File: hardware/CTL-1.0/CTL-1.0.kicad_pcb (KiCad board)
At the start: 2 copper layers, 139.7 x 63.5 mm, 58 parts, among them J1 Conn_02x16_Top_Bottom, J10 Conn_02x06_Odd_Even, J2 Conn_02x05_Odd_Even, J3 Conn_01x03, J4 Conn_01x02, J5 Conn_02x06_Odd_Even, J6 Conn_01x04, J7 Conn_01x04, J8 Conn_01x04, J9 Conn_01x06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

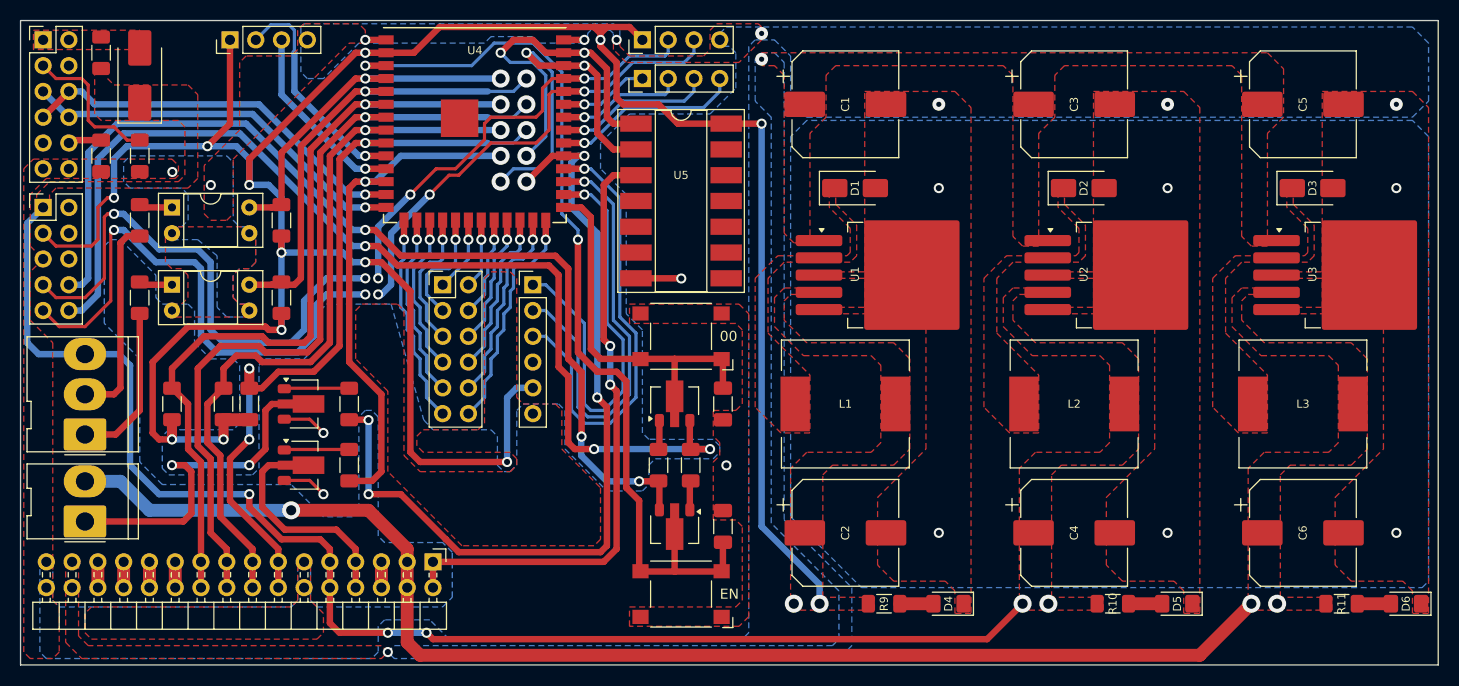
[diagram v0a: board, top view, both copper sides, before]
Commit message: modified:   .DS_Store 	modified:   README.md 	deleted:    hardware/CTL-1.0/CTL-1.0-backups/CTL-1.0-2025-05-23_140814.zip 	deleted:    hardware/CTL-1.0/CTL-1.0-backups/CTL-1.0-2025-05-23_142136.zip 	deleted:    hardware/CTL-1.0/CTL-1.0-backups/CTL-1.0-2025-05-23_145207.zip 	deleted:    hardware/CTL-1.0/CTL-1.0-backups/CTL-1.0-2025-05-23_145749.zip 	deleted:    hardware/CTL-1.0/CTL-1.0-backups/CTL-1.0-2025-06-03_185115.zip 	new file:   hardware/CTL-1.0/CTL-1.0-backups/CTL-1.0-2025-06-04_091843.zip 	new file:   hardware/CTL-1.0/CTL-1.0-backups/CTL-1.0-2025-06-04_105408.zip 	new file:   hardware/CTL-1.0/CTL-1.0-backups/CTL-1.0-2025-06-04_105918.zip 	new file:   hardware/CTL-1.0/CTL-1.0-backups/CTL-1.0-2025-06-04_110436.zip 	new file:   hardware/CTL-1.0/CTL-1.0-backups/CTL-1.0-2025-06-04_115049.zip 	new file:   hardware/CTL-1.0/CTL-1.0-backups/CTL-1.0-2025-06-04_132910.zip 	modified:   hardware/CTL-1.0/CTL-1.0.kicad_pcb 	modified:   hardware/CTL-1.0/CTL-1.0.kicad_prl 	modified:   hardware/CTL-1.0/CTL-1.0.kicad_sch 	new file:   hardware/PS-2.0/PS-2.0-backups/PS-2.0-2025-06-04_100004.zip 	new file:   hardware/PS-2.0/PS-2.0-backups/PS-2.0-2025-06-04_102434.zip 	new file:   hardware/PS-2.0/PS-2.0-backups/PS-2.0-2025-06-04_104734.zip 	new file:   hardware/PS-2.0/PS-2.0-backups/PS-2.0-2025-06-04_133345.zip 	modified:   hardware/PS-2.0/PS-2.0.kicad_pcb 	modified:   hardware/PS-2.0/PS-2.0.kicad_prl 	modified:   hardware/PS-2.0/PS-2.0.kicad_sch 	new file:   hardware/PS-2.0/~PS-2.0.kicad_pcb.lck 	new file:   hardware/PS-2.0/~PS-2.0.kicad_sch.lck 	modified:   pic/.DS_Store 	new file:   pic/PWM/Wave-pure-cut-driver-mosfet.png 	renamed:    pic/PWM/blend-cut-1/blend-cut-1-10.csv -> pic/PWM/blend-cut-1/CTL/blend-cut-1-10.csv 	renamed:    pic/PWM/blend-cut-1/blend-cut-1-10.png -> pic/PWM/blend-cut-1/CTL/blend-cut-1-10.png 	renamed:    pic/PWM/blend-cut-1/blend-cut-1-100.csv -> pic/PWM/blend-cut-1/CTL/blend-cut-1-100.csv 	renamed:    pic/PWM/blend-cut-1/blend-cut-1-100.png -> pic/PWM/ble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
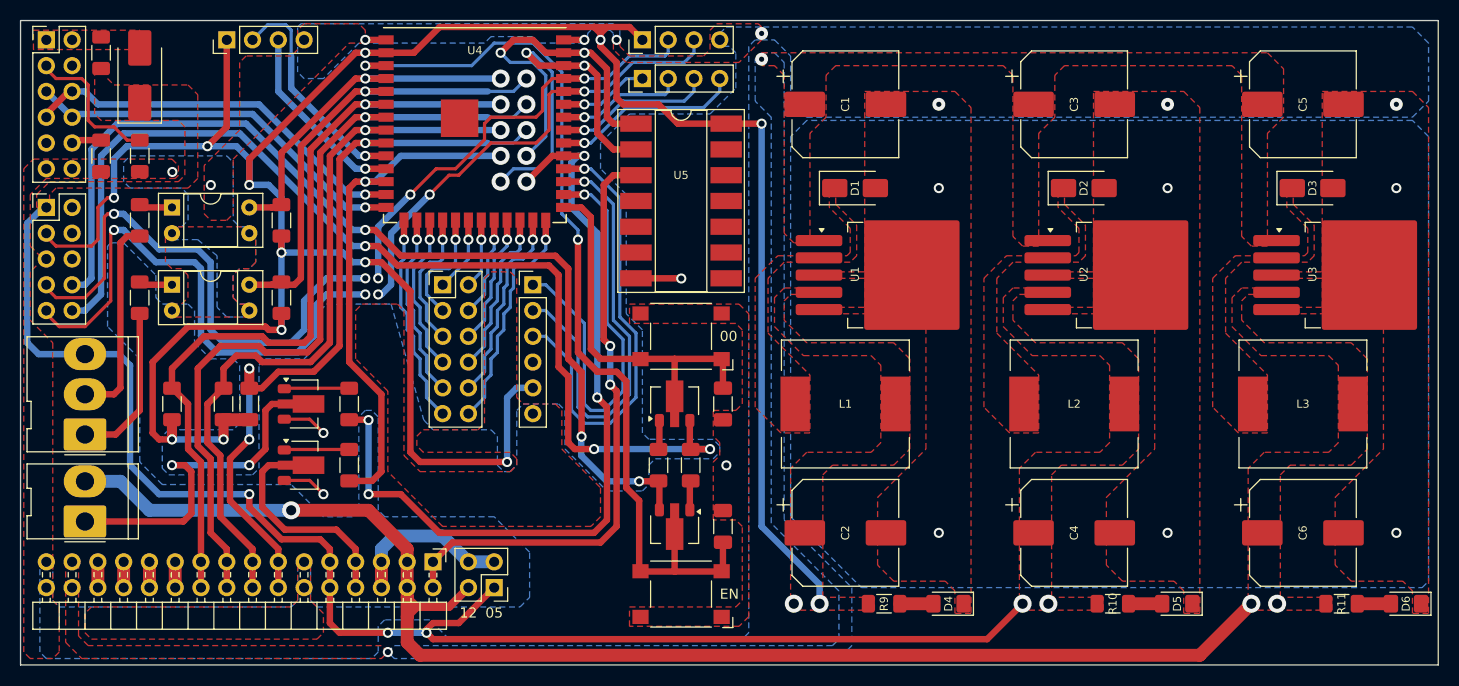
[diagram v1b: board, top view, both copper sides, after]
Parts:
- added J11: Conn_02x02_Odd_Even, Connector_PinHeader_2.54mm:PinHeader_2x02_P2.54mm_Vertical, F.Cu at (78.4, 151.1)
- moved J2 0.32 mm to (34.3, 113.7)
- moved J5 0.32 mm to (34.3, 97.2)
- moved J8 0.32 mm to (52.1, 97.2)
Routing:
- net /RLY-A: track 2.54 -> 16.5 mm
- net +5V: track 136.5 -> 145.2 mm
- net +12V: track 129.5 -> 138.1 mm
- net /CTL-BUZZ: track 83.0 -> 80.0 mm
- net /PWM: track 61.1 -> 59.8 mm
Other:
- board text added: "05"
- board text added: "12"

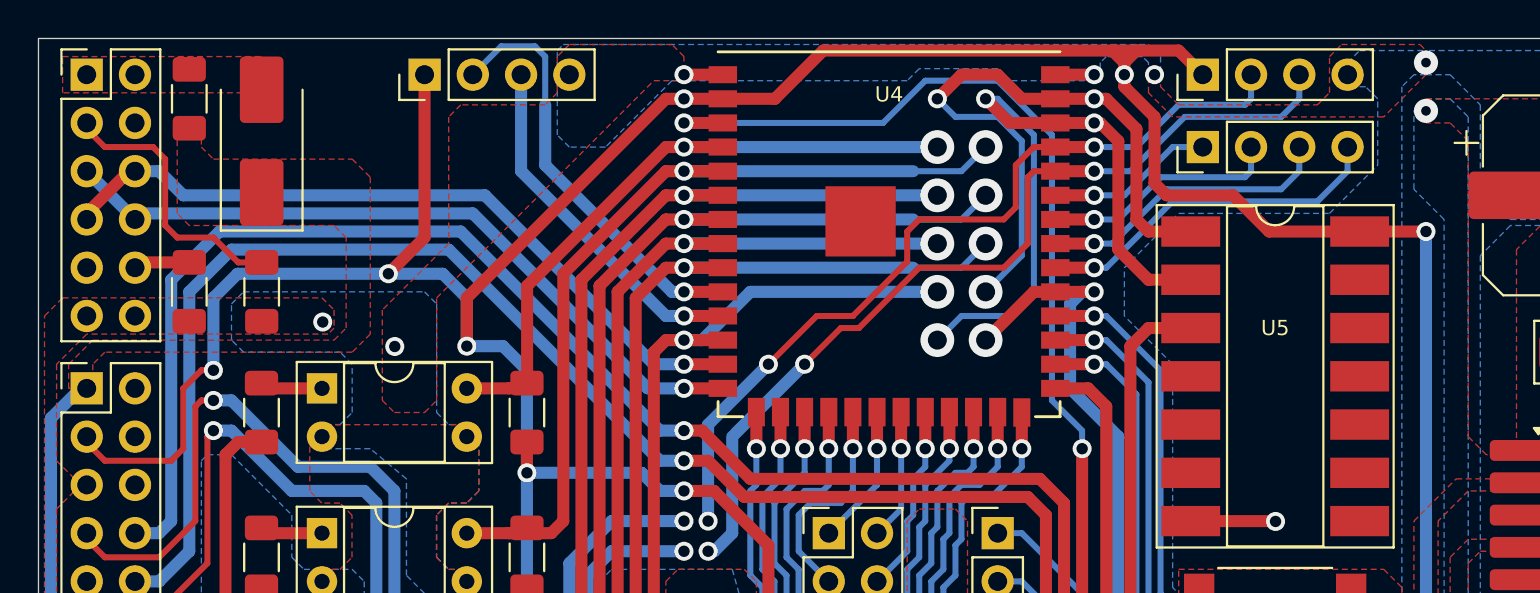
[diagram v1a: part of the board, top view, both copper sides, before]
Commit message: modified:   README.md 	deleted:    hardware/CTL-1.0/CTL-1.0-backups/CTL-1.0-2025-05-27_175205.zip 	deleted:    hardware/CTL-1.0/CTL-1.0-backups/CTL-1.0-2025-05-27_180035.zip 	deleted:    hardware/CTL-1.0/CTL-1.0-backups/CTL-1.0-2025-05-27_181441.zip 	deleted:    hardware/CTL-1.0/CTL-1.0-backups/CTL-1.0-2025-05-27_182529.zip 	deleted:    hardware/CTL-1.0/CTL-1.0-backups/CTL-1.0-2025-05-27_183819.zip 	deleted:    hardware/CTL-1.0/CTL-1.0-backups/CTL-1.0-2025-05-28_201558.zip 	deleted:    hardware/CTL-1.0/CTL-1.0-backups/CTL-1.0-2025-06-04_091843.zip 	new file:   hardware/CTL-1.0/CTL-1.0-backups/CTL-1.0-2025-06-05_141632.zip 	new file:   hardware/CTL-1.0/CTL-1.0-backups/CTL-1.0-2025-06-05_142549.zip 	new file:   hardware/CTL-1.0/CTL-1.0-backups/CTL-1.0-2025-06-05_143053.zip 	new file:   hardware/CTL-1.0/CTL-1.0-backups/CTL-1.0-2025-06-05_144242.zip 	new file:   hardware/CTL-1.0/CTL-1.0-backups/CTL-1.0-2025-06-05_144757.zip 	new file:   hardware/CTL-1.0/CTL-1.0-backups/CTL-1.0-2025-06-05_145506.zip 	modified:   hardware/CTL-1.0/CTL-1.0.kicad_pcb 	modified:   hardware/CTL-1.0/CTL-1.0.kicad_prl 	modified:   hardware/CTL-1.0/CTL-1.0.kicad_sch 	modified:   hardware/CTL-1.0/fp-info-cache 	new file:   hardware/PS-2.0/PS-2.0-backups/PS-2.0-2025-06-05_110653.zip 	new file:   hardware/PS-2.0/PS-2.0-backups/PS-2.0-2025-06-05_111332.zip 	new file:   hardware/PS-2.0/PS-2.0-backups/PS-2.0-2025-06-05_115228.zip 	new file:   hardware/PS-2.0/PS-2.0-backups/PS-2.0-2025-06-05_125334.zip 	modified:   hardware/PS-2.0/PS-2.0.kicad_pcb 	modified:   hardware/PS-2.0/PS-2.0.kicad_prl 	modified:   hardware/PS-2.0/PS-2.0.kicad_sch 	deleted:    hardware/PS-2.0/~PS-2.0.kicad_pcb.lck 	deleted:    hardware/PS-2.0/~PS-2.0.kicad_sch.lck 	modified:   pic/.DS_Store
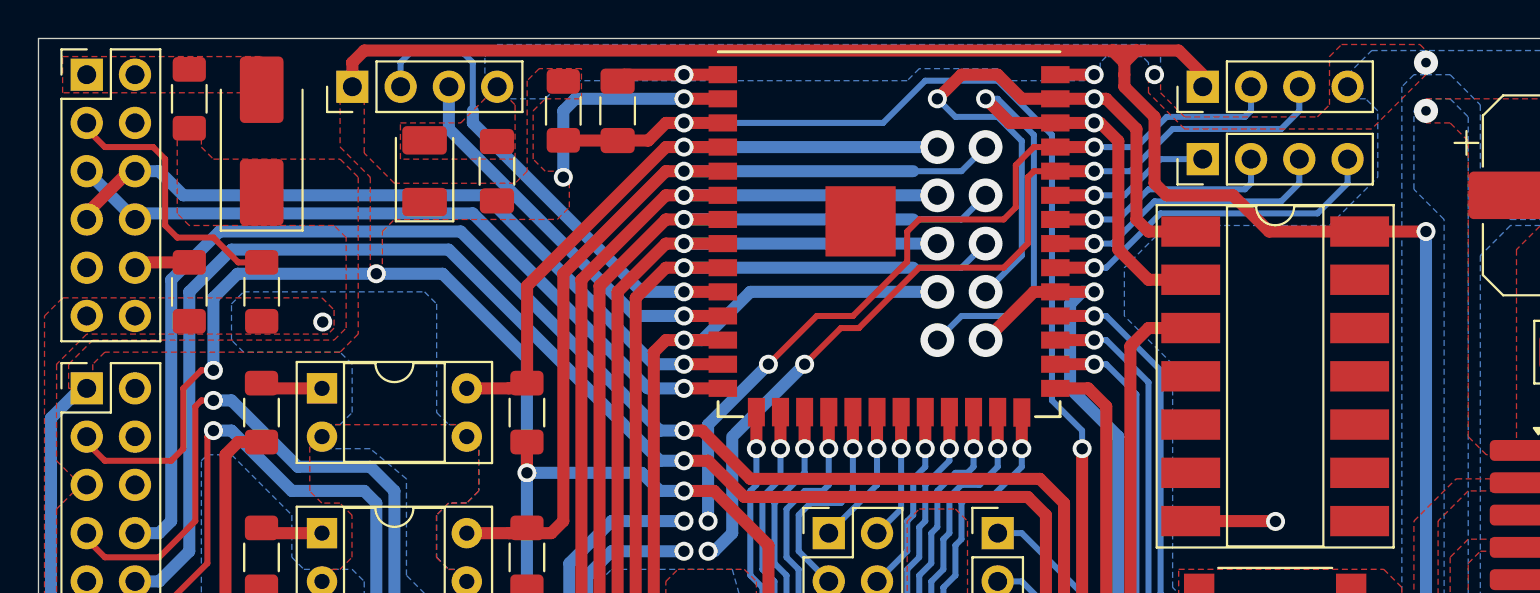
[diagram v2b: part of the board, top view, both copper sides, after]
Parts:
- added C10: 22µF 10V, Capacitor_Tantalum_SMD:CP_EIA-3528-12_Kemet-T_Pad1.50x2.35mm_HandSolder, F.Cu at (52.1, 102.2)
- added C11: 100nF, Capacitor_SMD:C_1206_3216Metric_Pad1.33x1.80mm_HandSolder, F.Cu at (55.9, 102.2)
- added C9: 1µF, Capacitor_SMD:C_1206_3216Metric_Pad1.33x1.80mm_HandSolder, F.Cu at (62.2, 99.1)
- added R16: 10k, Resistor_SMD:R_1206_3216Metric_Pad1.30x1.75mm_HandSolder, F.Cu at (59.4, 99.1)
- moved J8 3.85 mm to (48.3, 97.8)
- moved J6 0.64 mm to (93.0, 97.8)
- moved J7 0.63 mm to (93.0, 101.6)
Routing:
- net /EN: track 93.9 -> 101.3 mm
- net GND: track 17.6 -> 21.2 mm, vias 19 -> 18
- net /TXD.1: track 22.5 -> 25.6 mm
- net /RXD.1: track 18.9 -> 20.7 mm
- net +3.3V: track 268.7 -> 268.1 mm, vias 14 -> 13

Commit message: modified:   README.md 	deleted:    hardware/CTL-1.0/CTL-1.0-backups/CTL-1.0-2025-05-28_203806.zip 	deleted:    hardware/CTL-1.0/CTL-1.0-backups/CTL-1.0-2025-05-28_204313.zip 	deleted:    hardware/CTL-1.0/CTL-1.0-backups/CTL-1.0-2025-05-30_173028.zip 	deleted:    hardware/CTL-1.0/CTL-1.0-backups/CTL-1.0-2025-05-30_174116.zip 	deleted:    hardware/CTL-1.0/CTL-1.0-backups/CTL-1.0-2025-05-30_175122.zip 	new file:   hardware/CTL-1.0/CTL-1.0-backups/CTL-1.0-2025-07-24_151142.zip 	new file:   hardware/CTL-1.0/CTL-1.0-backups/CTL-1.0-2025-07-24_172002.zip 	new file:   hardware/CTL-1.0/CTL-1.0-backups/CTL-1.0-2025-07-25_175122.zip 	new file:   hardware/CTL-1.0/CTL-1.0-backups/CTL-1.0-2025-07-26_120011.zip 	new file:   hardware/CTL-1.0/CTL-1.0-backups/CTL-1.0-2025-07-26_120808.zip 	modified:   hardware/CTL-1.0/CTL-1.0.kicad_pcb 	modified:   hardware/CTL-1.0/CTL-1.0.kicad_pro 	new file:   hardware/CTL-1.0/CTL-1.0.step 	deleted:    hardware/MSD-1.0/MSD-1.0-backups/MSD-1.0-2025-04-11_111943.zip 	deleted:    hardware/MSD-1.0/MSD-1.0-backups/MSD-1.0-2025-04-11_113401.zip 	new file:   hardware/MSD-1.0/MSD-1.0-backups/MSD-1.0-2025-07-25_163151.zip 	new file:   hardware/MSD-1.0/MSD-1.0-backups/MSD-1.0-2025-07-25_171843.zip 	modified:   hardware/MSD-1.0/MSD-1.0.kicad_pcb 	modified:   hardware/MSD-1.0/MSD-1.0.step 	new file:   hardware/MSD-1.1/MSD-1.1-backups/MSD-1.1-2025-07-24_151252.zip 	new file:   hardware/MSD-1.1/MSD-1.1-backups/MSD-1.1-2025-07-25_152939.zip 	new file:   hardware/MSD-1.1/MSD-1.1-backups/MSD-1.1-2025-07-25_162346.zip 	new file:   hardware/MSD-1.1/MSD-1.1-backups/MSD-1.1-2025-07-25_162917.zip 	modified:   hardware/MSD-1.1/MSD-1.1.kicad_pcb 	modified:   hardware/MSD-1.1/MSD-1.1.step 	modified:   hardware/MSD-1.1/fp-info-cache 	new file:   hardware/MSD-2.0/MSD-2.0-backups/MSD-2.0-2025-07-24_151230.zip 	deleted:    hardware/PS-2.0/PS-2.0-backups/PS-2.0-2025-05-07_010425.zip 	deleted:    hardware/PS-2.0/PS-2.0-backups/PS-2.0-2025-05-09_084820.zip 	deleted:    hardware/P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
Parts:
- moved C2 1.27 mm to (113.0, 144.5)
- moved C4 1.27 mm to (135.6, 144.5)
- moved C6 1.27 mm to (158.1, 144.5)
- moved L1 0.63 mm to (113.0, 132.4)
- moved L2 0.63 mm to (135.6, 132.4)
- moved L3 0.63 mm to (158.1, 132.4)
- moved U1 0.63 mm to (118.1, 119.7)
- moved U2 0.63 mm to (140.6, 119.7)
- moved U3 0.63 mm to (163.2, 119.7)

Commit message: deleted:    hardware/CTL-1.0/CTL-1.0-backups/CTL-1.0-2025-06-04_115049.zip 	deleted:    hardware/CTL-1.0/CTL-1.0-backups/CTL-1.0-2025-06-04_132910.zip 	deleted:    hardware/CTL-1.0/CTL-1.0-backups/CTL-1.0-2025-06-05_142549.zip 	deleted:    hardware/CTL-1.0/CTL-1.0-backups/CTL-1.0-2025-06-05_143053.zip 	deleted:    hardware/CTL-1.0/CTL-1.0-backups/CTL-1.0-2025-06-05_144242.zip 	new file:   hardware/CTL-1.0/CTL-1.0-backups/CTL-1.0-2025-08-01_111317.zip 	new file:   hardware/CTL-1.0/CTL-1.0-backups/CTL-1.0-2025-08-01_113544.zip 	new file:   hardware/CTL-1.0/CTL-1.0-backups/CTL-1.0-2025-08-01_114559.zip 	new file:   hardware/CTL-1.0/CTL-1.0-backups/CTL-1.0-2025-08-01_115359.zip 	new file:   hardware/CTL-1.0/CTL-1.0-backups/CTL-1.0-2025-08-01_115915.zip 	new file:   hardware/CTL-1.0/CTL-1.0-backups/CTL-1.0-2025-08-01_131607.zip 	modified:   hardware/CTL-1.0/CTL-1.0.kicad_pcb 	modified:   hardware/CTL-1.0/CTL-1.0.kicad_sch 	renamed:    hardware/CTL-1.0/CTL-1.0-backups/CTL-1.0-2025-06-05_144757.zip -> hardware/CTL-1.2/CTL-1.0-backups/CTL-1.0-2025-06-05_145506.zip 	new file:   hardware/CTL-1.2/CTL-1.0-backups/CTL-1.0-2025-06-10_100335.zip 	new file:   hardware/CTL-1.2/CTL-1.0-backups/CTL-1.0-2025-06-12_095314.zip 	new file:   hardware/CTL-1.2/CTL-1.0-backups/CTL-1.0-2025-07-03_115731.zip 	new file:   hardware/CTL-1.2/CTL-1.0-backups/CTL-1.0-2025-07-16_143147.zip 	new file:   hardware/CTL-1.2/CTL-1.0-backups/CTL-1.0-2025-07-24_151142.zip 	new file:   hardware/CTL-1.2/CTL-1.0-backups/CTL-1.0-2025-07-24_172002.zip 	new file:   hardware/CTL-1.2/CTL-1.0-backups/CTL-1.0-2025-07-25_175122.zip 	new file:   hardware/CTL-1.2/CTL-1.0-backups/CTL-1.0-2025-07-26_120011.zip 	new file:   hardware/CTL-1.2/CTL-1.0-backups/CTL-1.0-2025-07-26_120808.zip 	new file:   hardware/CTL-1.2/CTL-1.0-backups/CTL-1.0-2025-07-28_094555.zip 	new file:   hardware/CTL-1.2/CTL-1.0-backups/CTL-1.0-2025-07-28_104747.zip 	new file:   hardware/CTL-1.2/CTL-1.0-backups/CTL-1.0-2025-07-28_112613.zip 	new file:   ha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
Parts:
- added K1: G5V-1, Relay_THT:Relay_SPDT_Omron_G5V-1, F.Cu at (87.3, 153.7)
- added Q5: BCX56, Package_TO_SOT_SMD:SOT-89-3, F.Cu at (77.2, 143.5)
- added R19: 10k, Resistor_SMD:R_1206_3216Metric_Pad1.30x1.75mm_HandSolder, F.Cu at (72.4, 143.5)
- D7: value D -> BAT60A
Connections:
- net /SEN-BI renamed /SEN-COAG
- net /SEN-MONO renamed /SEN-CUT
- net /SW-BI renamed /SW-COAG
- net /SW-MONO renamed /SW-CUT
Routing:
- net /CTL-BUZZ: track 80.0 -> 72.9 mm
- net Net-(Q5-B): track 0.00 -> 6.73 mm
- net +3.3V: track 268.1 -> 262.8 mm
